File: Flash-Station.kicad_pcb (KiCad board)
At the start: 2 copper layers, 31.2 x 39.4 mm, 7 parts, among them J1 Vin 3.3V, J2 FTDI, J3 ISP, J4 HMSensor Pogo 2, J5 HMSensor Pogo 1, J6 VCC Jumper, SW1 VCC Switch

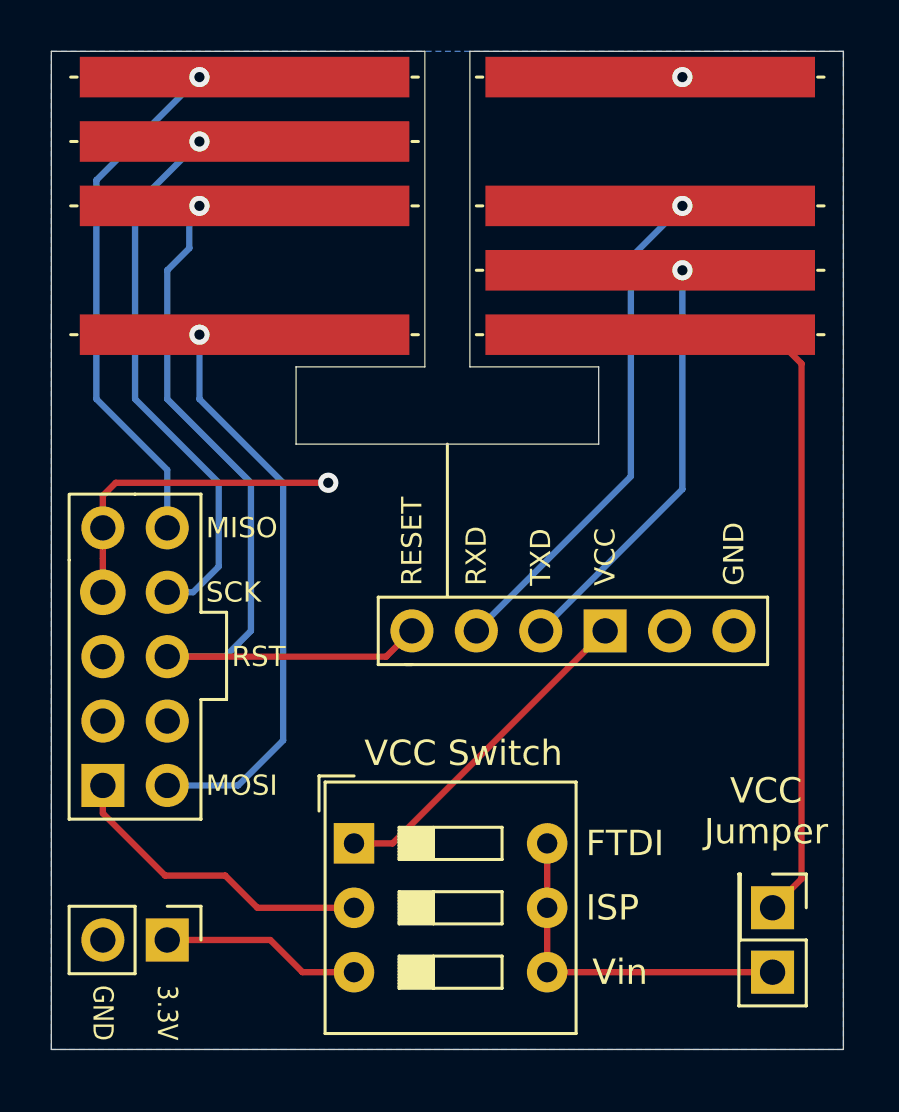
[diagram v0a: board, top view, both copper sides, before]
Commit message: Fix: Tx/RX interchanged, RESET Kerko
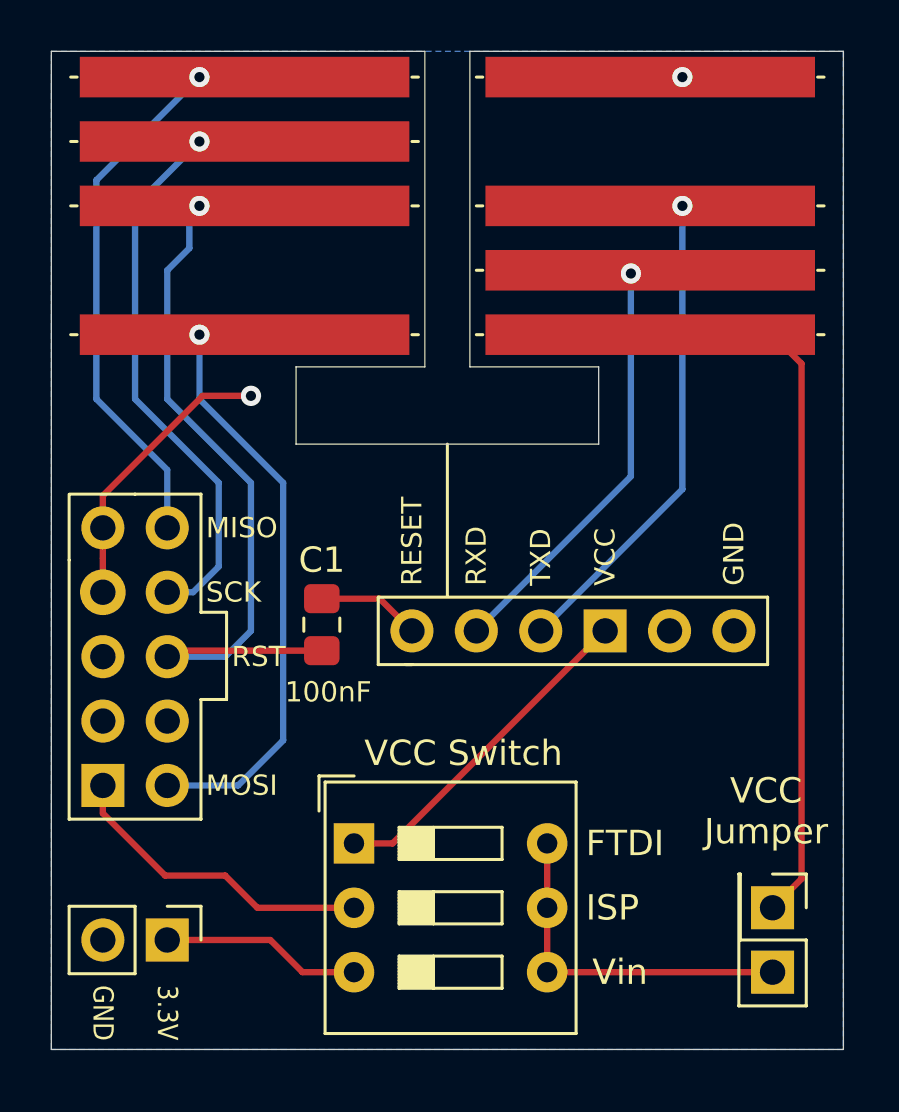
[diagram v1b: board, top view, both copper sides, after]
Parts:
- added C1: 100nF, Capacitor_SMD:C_0805_2012Metric_Pad1.15x1.40mm_HandSolder, F.Cu at (77.2, 81.3)
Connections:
- J2 pad 1: RESET -> Net-(C1-Pad2)
- J2 pad 2: RXD -> TXD
- J2 pad 3: TXD -> RXD
- J3 pad 5: (no net) -> Net-(J3-Pad5)
- J3 pad 7: (no net) -> Net-(J3-Pad7)
- J3 pad 8: (no net) -> Net-(J3-Pad8)
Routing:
- net Net-(C1-Pad2): track 0.00 -> 4.12 mm
- net RESET: track 32.5 -> 28.6 mm
- net GND: track 12.9 -> 10.9 mm
- net RXD: track 20.1 -> 19.1 mm
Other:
- board text added: "HMSensor FlashStation v1.1 by Christoph Wiechert"

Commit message: Fix Schaltplan
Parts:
- moved C1 0.25 mm to (77.5, 81.3), turned to 270 degrees
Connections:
- C1 pad 1: RESET -> Net-(C1-Pad1)
- C1 pad 2: Net-(C1-Pad2) -> RESET
- J2 pad 1: Net-(C1-Pad2) -> Net-(C1-Pad1)
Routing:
- net Net-(C1-Pad2): track 4.12 -> 0.00 mm
- net Net-(C1-Pad1): track 0.00 -> 4.12 mm
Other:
- board text added: "100nF"
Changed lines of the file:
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@@
   (general
     (thickness 1.6)
-    (drawings 29)
+    (drawings 32)
     (tracks 60)
     (zones 0)
@@
   (net 12 "Net-(J2-Pad4)")
   (net 13 "Net-(J3-Pad9)")
-  (net 14 "Net-(C1-Pad2)")
-  (net 15 "Net-(J3-Pad8)")
-  (net 16 "Net-(J3-Pad7)")
-  (net 17 "Net-(J3-Pad5)")
+  (net 14 "Net-(J3-Pad8)")
+  (net 15 "Net-(J3-Pad7)")
+  (net 16 "Net-(J3-Pad5)")
+  (net 17 "Net-(C1-Pad1)")
   (net_class Default "Dies ist die voreingestellte Netzklasse."
     (clearance 0.2)
@@
     (add_net MISO)
     (add_net MOSI)
-    (add_net "Net-(C1-Pad2)")
+    (add_net "Net-(C1-Pad1)")
     (add_net "Net-(J1-Pad1)")
     (add_net "Net-(J2-Pad4)")
@@
     (add_net TXD)
     (add_net VCC)
-  )
-  (module Capacitor_SMD:C_0805_2012Metric_Pad1.15x1.40mm_HandSolder (layer F.Cu)
-    (at 77.216 81.289 90)
-    (descr "Capacitor SMD 0805 (2012 Metric), square (rectangular) end terminal, IPC_7351 nominal with elongated pad for handsoldering. (Body size source: https://docs.google.com/spreadsheets/d/1BsfQQcO9C6DZCsRaXUlFlo91Tg2WpOkGARC1WS5S8t0/edit?usp=sharing), generated with kicad-footprint-generator")
-    (tags "capacitor handsolder")
-    (attr smd)
-    (fp_text reference C1 (at 2.549 0 180) (layer F.SilkS)
-      (effects (font (size 1 1) (thickness 0.15)))
-    )
-    (fp_text value 100nF (at -2.658 0.254 180) (layer F.SilkS)
-      (effects (font (size 0.8 0.8) (thickness 0.15)))
-    )
-    (fp_text user %R (at 0 0 90) (layer F.Fab)
-      (effects (font (size 0.5 0.5) (thickness 0.08)))
-    )
-    (fp_line (start 1.85 0.95) (end -1.85 0.95) (layer F.CrtYd) (width 0.05))
-    (fp_line (start 1.85 -0.95) (end 1.85 0.95) (layer F.CrtYd) (width 0.05))
-    (fp_line (start -1.85 -0.95) (end 1.85 -0.95) (layer F.CrtYd) (width 0.05))
-    (fp_line (start -1.85 0.95) (end -1.85 -0.95) (layer F.CrtYd) (width 0.05))
-    (fp_line (start -0.261252 0.71) (end 0.261252 0.71) (layer F.SilkS) (width 0.12))
-    (fp_line (start -0.261252 -0.71) (end 0.261252 -0.71) (layer F.SilkS) (width 0.12))
-    (fp_line (start 1 0.6) (end -1 0.6) (layer F.Fab) (width 0.1))
-    (fp_line (start 1 -0.6) (end 1 0.6) (layer F.Fab) (width 0.1))
-    (fp_line (start -1 -0.6) (end 1 -0.6) (layer F.Fab) (width 0.1))
-    (fp_line (start -1 0.6) (end -1 -0.6) (layer F.Fab) (width 0.1))
-    (pad 2 smd roundrect (at 1.025 0 90) (size 1.15 1.4) (layers F.Cu F.Paste F.Mask) (roundrect_rratio 0.217391)
-      (net 14 "Net-(C1-Pad2)"))
-    (pad 1 smd roundrect (at -1.025 0 90) (size 1.15 1.4) (layers F.Cu F.Paste F.Mask) (roundrect_rratio 0.217391)
-      (net 5 RESET))
-    (model ${KISYS3DMOD}/Capacitor_SMD.3dshapes/C_0805_2012Metric.wrl
-      (at (xyz 0 0 0))
-      (scale (xyz 1 1 1))
-      (rotate (xyz 0 0 0))
-    )
   )
   (module Connector_PinHeader_2.54mm:PinHeader_1x06_P2.54mm_Vertical (layer F.Cu)
@@
       (net 9 TXD))
     (pad 1 thru_hole circle (at 0 0 90) (size 1.7 1.7) (drill 1) (layers *.Cu *.Mask)
-      (net 14 "Net-(C1-Pad2)"))
+      (net 17 "Net-(C1-Pad1)"))
     (model ${KISYS3DMOD}/Connector_PinHeader_2.54mm.3dshapes/PinHeader_1x06_P2.54mm_Vertical.wrl
       (at (xyz 0 0 0))
@@
       (net 13 "Net-(J3-Pad9)"))
     (pad 8 thru_hole oval (at 2.54 7.62) (size 1.7 1.7) (drill 1) (layers *.Cu *.Mask)
-      (net 15 "Net-(J3-Pad8)"))
+      (net 14 "Net-(J3-Pad8)"))
     (pad 7 thru_hole oval (at 0 7.62) (size 1.7 1.7) (drill 1) (layers *.Cu *.Mask)
-      (net 16 "Net-(J3-Pad7)"))
+      (net 15 "Net-(J3-Pad7)"))
     (pad 6 thru_hole oval (at 2.54 5.08) (size 1.7 1.7) (drill 1) (layers *.Cu *.Mask)
       (net 5 RESET))
     (pad 5 thru_hole oval (at 0 5.08) (size 1.7 1.7) (drill 1) (layers *.Cu *.Mask)
-      (net 17 "Net-(J3-Pad5)"))
+      (net 16 "Net-(J3-Pad5)"))
     (pad 4 thru_hole oval (at 2.54 2.54) (size 1.7 1.7) (drill 1) (layers *.Cu *.Mask)
       (net 4 SCK))
@@
     )
   )
+  (module Capacitor_SMD:C_0805_2012Metric_Pad1.15x1.40mm_HandSolder (layer F.Cu)
+    (at 77.47 81.28 270)
+    (descr "Capacitor SMD 0805 (2012 Metric), square (rectangular) end terminal, IPC_7351 nominal with elongated pad for handsoldering. (Body size source: https://docs.google.com/spreadsheets/d/1BsfQQcO9C6DZCsRaXUlFlo91Tg2WpOkGARC1WS5S8t0/edit?usp=sharing), generated with kicad-footprint-generator")
+    (tags "capacitor handsolder")
+    (attr smd)
+    (fp_text reference C1 (at -2.54 0 180) (layer F.SilkS)
+      (effects (font (size 1 1) (thickness 0.15)))
+    )
+    (fp_text value 100nF (at 0 1.65 90) (layer F.Fab)
+      (effects (font (size 1 1) (thickness 0.15)))
+    )
+    (fp_line (start -1 0.6) (end -1 -0.6) (layer F.Fab) (width 0.1))
+    (fp_line (start -1 -0.6) (end 1 -0.6) (layer F.Fab) (width 0.1))
+    (fp_line (start 1 -0.6) (end 1 0.6) (layer F.Fab) (width 0.1))
+    (fp_line (start 1 0.6) (end -1 0.6) (layer F.Fab) (width 0.1))
+    (fp_line (start -0.261252 -0.71) (end 0.261252 -0.71) (layer F.SilkS) (width 0.12))
+    (fp_line (start -0.261252 0.71) (end 0.261252 0.71) (layer F.SilkS) (width 0.12))
+    (fp_line (start -1.85 0.95) (end -1.85 -0.95) (layer F.CrtYd) (width 0.05))
+    (fp_line (start -1.85 -0.95) (end 1.85 -0.95) (layer F.CrtYd) (width 0.05))
+    (fp_line (start 1.85 -0.95) (end 1.85 0.95) (layer F.CrtYd) (width 0.05))
+    (fp_line (start 1.85 0.95) (end -1.85 0.95) (layer F.CrtYd) (width 0.05))
+    (fp_text user %R (at 0 0 90) (layer F.Fab)
+      (effects (font (size 0.5 0.5) (thickness 0.08)))
+    )
+    (pad 1 smd roundrect (at -1.025 0 270) (size 1.15 1.4) (layers F.Cu F.Paste F.Mask) (roundrect_rratio 0.217391)
+      (net 17 "Net-(C1-Pad1)"))
+    (pad 2 smd roundrect (at 1.025 0 270) (size 1.15 1.4) (layers F.Cu F.Paste F.Mask) (roundrect_rratio 0.217391)
+      (net 5 RESET))
+    (model ${KISYS3DMOD}/Capacitor_SMD.3dshapes/C_0805_2012Metric.wrl
+      (at (xyz 0 0 0))
+      (scale (xyz 1 1 1))
+      (rotate (xyz 0 0 0))
+    )
+  )
+  (gr_text VCC (at 67.31 89.535) (layer F.SilkS)
+    (effects (font (size 0.8 0.8) (thickness 0.15)) (justify left))
+  )
+  (gr_text GND (at 67.31 75.565) (layer F.SilkS)
+    (effects (font (size 0.8 0.8) (thickness 0.15)) (justify left))
+  )
+  (gr_text 100nF (at 75.565 83.82) (layer F.SilkS)
+    (effects (font (size 0.8 0.8) (thickness 0.15)) (justify left))
+  )
   (gr_text "HMSensor\nFlashStation\nv1.1\nby Christoph Wiechert" (at 93.091 77.089 270) (layer B.SilkS)
     (effects (font (size 1 1) (thickness 0.15)) (justify left mirror))
@@
   (segment (start 71.036 91.186) (end 68.58 88.73) (width 0.25) (layer F.Cu) (net 13))
   (segment (start 73.406 91.186) (end 71.036 91.186) (width 0.25) (layer F.Cu) (net 13))
-  (segment (start 80.481795 81.187795) (end 80.453795 81.215795) (width 0.25) (layer F.Cu) (net 14))
-  (segment (start 79.502 80.264) (end 77.216 80.264) (width 0.25) (layer F.Cu) (net 14))
-  (segment (start 80.772 81.534) (end 79.502 80.264) (width 0.25) (layer F.Cu) (net 14))
+  (segment (start 80.481795 81.187795) (end 80.453795 81.215795) (width 0.25) (layer F.Cu) (net 17))
+  (segment (start 79.502 80.264) (end 77.216 80.264) (width 0.25) (layer F.Cu) (net 17))
+  (segment (start 80.772 81.534) (end 79.502 80.264) (width 0.25) (layer F.Cu) (net 17))
   (zone (net 1) (net_name GND) (layer B.Cu) (hatch edge 0.508)
     (connect_pads (clearance 0.508))
